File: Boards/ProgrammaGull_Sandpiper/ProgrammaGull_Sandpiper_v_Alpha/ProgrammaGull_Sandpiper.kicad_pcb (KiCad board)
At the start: 4 copper layers, 100 x 75 mm, 191 parts, among them J4 Conn_01x22_Socket, P1 USB_C_Plug_USB2.0, Q1 MMBT2907, Q2 MMBT2907, Q3 MMBT2907, Q4 MMBT2907, Q5 MMBT2907, Q6 MMBT2907, Q7 MMBT2907, Q8 MMBT2907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

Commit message: Final Alpha Version
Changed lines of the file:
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@@
     (property "ki_keywords" "EEPROM memory Microwire")
     (attr smd)
-    (fp_text reference "U6" (at -2.7 -1.65 180) (layer "F.SilkS")
+    (fp_text reference "U6" (at 5.25 -6.8 180) (layer "F.SilkS")
         (effects (font (size 1 1) (thickness 0.15)))
     )
@@
     (property "ki_keywords" "HCMOS SR OpenCollector")
     (attr smd)
-    (fp_text reference "U3" (at 0 -3.45 90) (layer "F.SilkS")
+    (fp_text reference "U3" (at -1.6625 4.125 -180) (layer "F.SilkS")
         (effects (font (size 1 1) (thickness 0.15)))
     )

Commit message: Final Sandpiper Alpha Changes, just cleanup.
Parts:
- moved C33 1.95 mm to (94.5, 55.8)
- moved C32 1.80 mm to (92.5, 56.0)
- turned C3 to -90 degrees
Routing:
- net GND: track 119.4 -> 114.3 mm

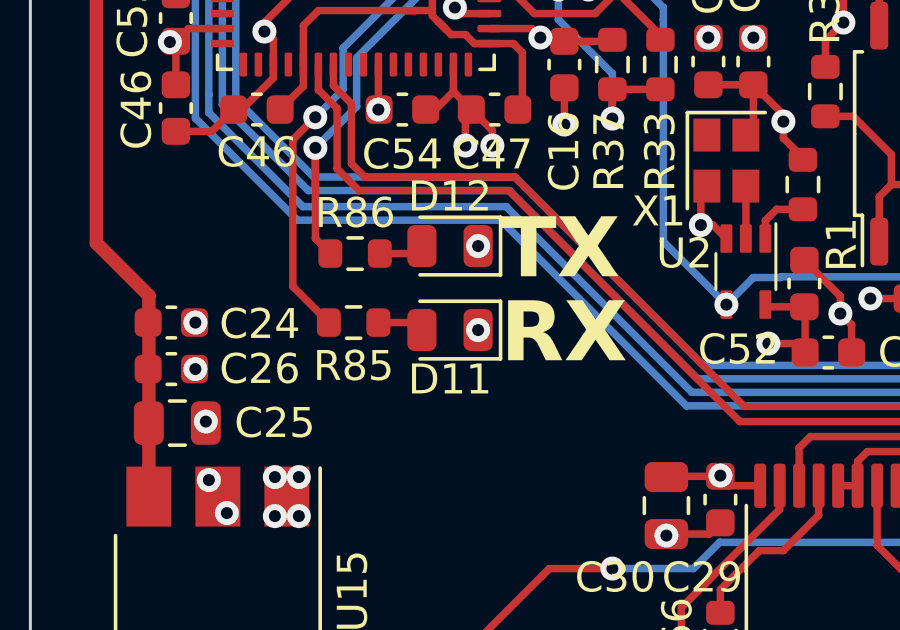
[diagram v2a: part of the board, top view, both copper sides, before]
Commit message: Errata: Fixed reversed LEDs on FTDI.... oops :)
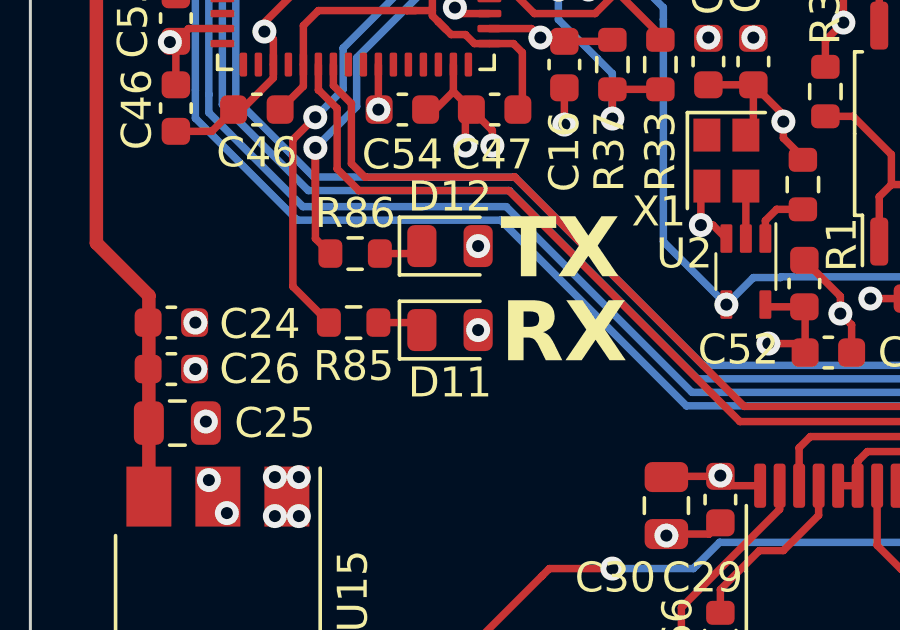
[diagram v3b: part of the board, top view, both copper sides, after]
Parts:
- turned D11 to 0 degrees
- turned D12 to 0 degrees
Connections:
- D11 pad 1: GND -> Net-(D11-K)
- D11 pad 2: Net-(D11-A) -> +3V3
- D12 pad 1: GND -> Net-(D12-K)
- D12 pad 2: Net-(D12-A) -> +3V3
- R85 pad 1: Net-(D11-A) -> Net-(D11-K)
- R86 pad 1: Net-(D12-A) -> Net-(D12-K)
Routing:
- net Net-(D11-K): track 0.00 -> 1.55 mm
- net Net-(D11-A): track 1.55 -> 0.00 mm
- net Net-(D12-K): track 0.00 -> 1.50 mm
- net Net-(D12-A): track 1.50 -> 0.00 mm
- net GND: vias 96 -> 94
- net +3V3: vias 54 -> 56
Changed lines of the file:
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@@
   (net 164 "Net-(J4-Pin_11)")
   (net 165 "Net-(J4-Pin_12)")
-  (net 166 "Net-(D11-A)")
-  (net 167 "Net-(D12-A)")
+  (net 166 "Net-(D11-K)")
+  (net 167 "Net-(D12-K)")
   (net 168 "Net-(U7-BCBUS4)")
   (net 169 "Net-(U7-BCBUS3)")
@@
       (stroke (width 0.1) (type solid)) (layer "F.Fab"))
     (pad "1" smd roundrect (at -0.825 0 180) (size 0.8 0.95) (layers "F.Cu" "F.Paste" "F.Mask") (roundrect_rratio 0.25)
-      (net 166 "Net-(D11-A)") (pintype "passive"))
+      (net 166 "Net-(D11-K)") (pintype "passive"))
     (pad "2" smd roundrect (at 0.825 0 180) (size 0.8 0.95) (layers "F.Cu" "F.Paste" "F.Mask") (roundrect_rratio 0.25)
       (net 168 "Net-(U7-BCBUS4)") (pintype "passive"))
@@
   )
   (footprint "LED_SMD:LED_0805_2012Metric" (layer "F.Cu")
-    (at 38.9875 64.25 180)
+    (at 38.9875 64.25)
     (descr "LED SMD 0805 (2012 Metric), square (rectangular) end terminal, IPC_7351 nominal, (Body size source: https://docs.google.com/spreadsheets/d/1BsfQQcO9C6DZCsRaXUlFlo91Tg2WpOkGARC1WS5S8t0/edit?usp=sharing), generated with kicad-footprint-generator")
     (tags "LED")
@@
     (property "ki_keywords" "LED diode")
     (attr smd)
-    (fp_text reference "D11" (at 0 -1.65) (layer "F.SilkS")
+    (fp_text reference "D11" (at 0 1.75) (layer "F.SilkS")
         (effects (font (size 1 1) (thickness 0.15)))
     )
@@
     (fp_line (start 1 0.6) (end 1 -0.6)
       (stroke (width 0.1) (type solid)) (layer "F.Fab"))
-    (pad "1" smd roundrect (at -0.9375 0 180) (size 0.975 1.4) (layers "F.Cu" "F.Paste" "F.Mask") (roundrect_rratio 0.25)
-      (net 2 "GND") (pinfunction "K") (pintype "passive"))
-    (pad "2" smd roundrect (at 0.9375 0 180) (size 0.975 1.4) (layers "F.Cu" "F.Paste" "F.Mask") (roundrect_rratio 0.25)
-      (net 166 "Net-(D11-A)") (pinfunction "A") (pintype "passive"))
+    (pad "1" smd roundrect (at -0.9375 0) (size 0.975 1.4) (layers "F.Cu" "F.Paste" "F.Mask") (roundrect_rratio 0.25)
+      (net 166 "Net-(D11-K)") (pinfunction "K") (pintype "passive"))
+    (pad "2" smd roundrect (at 0.9375 0) (size 0.975 1.4) (layers "F.Cu" "F.Paste" "F.Mask") (roundrect_rratio 0.25)
+      (net 3 "+3V3") (pinfunction "A") (pintype "passive"))
     (model "${KICAD6_3DMODEL_DIR}/LED_SMD.3dshapes/LED_0805_2012Metric.wrl"
       (offset (xyz 0 0 0))
@@
       (stroke (width 0.1) (type solid)) (layer "F.Fab"))
     (pad "1" smd roundrect (at -0.825 0 180) (size 0.8 0.95) (layers "F.Cu" "F.Paste" "F.Mask") (roundrect_rratio 0.25)
-      (net 167 "Net-(D12-A)") (pintype "passive"))
+      (net 167 "Net-(D12-K)") (pintype "passive"))
     (pad "2" smd roundrect (at 0.825 0 180) (size 0.8 0.95) (layers "F.Cu" "F.Paste" "F.Mask") (roundrect_rratio 0.25)
       (net 169 "Net-(U7-BCBUS3)") (pintype "passive"))
@@
   )
   (footprint "LED_SMD:LED_0805_2012Metric" (layer "F.Cu")
-    (at 38.9875 61.45 180)
+    (at 38.9875 61.45)
     (descr "LED SMD 0805 (2012 Metric), square (rectangular) end terminal, IPC_7351 nominal, (Body size source: https://docs.google.com/spreadsheets/d/1BsfQQcO9C6DZCsRaXUlFlo91Tg2WpOkGARC1WS5S8t0/edit?usp=sharing), generated with kicad-footprint-generator")
     (tags "LED")
@@
     (property "ki_keywords" "LED diode")
     (attr smd)
-    (fp_text reference "D12" (at 0 1.65) (layer "F.SilkS")
+    (fp_text reference "D12" (at 0 -1.65) (layer "F.SilkS")
         (effects (font (size 1 1) (thickness 0.15)))
     )
@@
     (fp_line (start 1 0.6) (end 1 -0.6)
       (stroke (width 0.1) (type solid)) (layer "F.Fab"))
-    (pad "1" smd roundrect (at -0.9375 0 180) (size 0.975 1.4) (layers "F.Cu" "F.Paste" "F.Mask") (roundrect_rratio 0.25)
-      (net 2 "GND") (pinfunction "K") (pintype "passive"))
-    (pad "2" smd roundrect (at 0.9375 0 180) (size 0.975 1.4) (layers "F.Cu" "F.Paste" "F.Mask") (roundrect_rratio 0.25)
-      (net 167 "Net-(D12-A)") (pinfunction "A") (pintype "passive"))
+    (pad "1" smd roundrect (at -0.9375 0) (size 0.975 1.4) (layers "F.Cu" "F.Paste" "F.Mask") (roundrect_rratio 0.25)
+      (net 167 "Net-(D12-K)") (pinfunction "K") (pintype "passive"))
+    (pad "2" smd roundrect (at 0.9375 0) (size 0.975 1.4) (layers "F.Cu" "F.Paste" "F.Mask") (roundrect_rratio 0.25)
+      (net 3 "+3V3") (pinfunction "A") (pintype "passive"))
     (model "${KICAD6_3DMODEL_DIR}/LED_SMD.3dshapes/LED_0805_2012Metric.wrl"
       (offset (xyz 0 0 0))
@@
   (via (at 35.15 52.75) (size 0.8) (drill 0.4) (layers "F.Cu" "B.Cu") (net 2))
   (via (at 38.6 40.6) (size 0.8) (drill 0.4) (layers "F.Cu" "B.Cu") (free) (net 2))
-  (via (at 39.925 64.25) (size 0.8) (drill 0.4) (layers "F.Cu" "B.Cu") (net 2))
   (via (at 39.5 58.1) (size 0.8) (drill 0.4) (layers "F.Cu" "B.Cu") (free) (net 2))
   (via (at 71 76.1) (size 0.8) (drill 0.4) (layers "F.Cu" "B.Cu") (net 2))
@@
   (via (at 58.6 61.3) (size 0.8) (drill 0.4) (layers "F.Cu" "B.Cu") (free) (net 2))
   (via (at 112.3975 76.33) (size 0.8) (drill 0.4) (layers "F.Cu" "B.Cu") (free) (net 2))
-  (via (at 39.925 61.45) (size 0.8) (drill 0.4) (layers "F.Cu" "B.Cu") (net 2))
   (via (at 78.3 72.9) (size 0.8) (drill 0.4) (layers "F.Cu" "B.Cu") (net 2))
   (via (at 66.5 83.3) (size 0.8) (drill 0.4) (layers "F.Cu" "B.Cu") (net 2))
@@
   (via (at 41.95 39.35) (size 0.8) (drill 0.4) (layers "F.Cu" "B.Cu") (free) (net 3))
   (via (at 67.1 74.3) (size 0.8) (drill 0.4) (layers "F.Cu" "B.Cu") (net 3))
+  (via (at 39.925 64.25) (size 0.8) (drill 0.4) (layers "F.Cu" "B.Cu") (net 3))
   (via (at 118.1 86.9) (size 0.8) (drill 0.4) (layers "F.Cu" "B.Cu") (net 3))
   (via (at 59.925 75) (size 0.8) (drill 0.4) (layers "F.Cu" "B.Cu") (free) (net 3))
@@
   (via (at 55.2 70.6) (size 0.8) (drill 0.4) (layers "F.Cu" "B.Cu") (net 3))
   (via (at 30.65 75.55) (size 0.8) (drill 0.4) (layers "F.Cu" "B.Cu") (net 3))
+  (via (at 39.925 61.45) (size 0.8) (drill 0.4) (layers "F.Cu" "B.Cu") (net 3))
   (via (at 76.7 72.9) (size 0.8) (drill 0.4) (layers "F.Cu" "B.Cu") (net 3))
   (via (at 59.725 71.65) (size 0.8) (drill 0.4) (layers "F.Cu" "B.Cu") (net 3))

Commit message: Updated board revision for Alpha
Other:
- board text added: "Version: Alpha 0.2"
- board text removed: "Version: Alpha 0.1"
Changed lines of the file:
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@@
     (effects (font (size 1.5 1.5) (thickness 0.3) bold) (justify left bottom mirror))
   )
-  (gr_text "Version: Alpha 0.1" (at 95 75.45) (layer "B.SilkS")
+  (gr_text "Version: Alpha 0.2" (at 95 75.45) (layer "B.SilkS")
     (effects (font (size 2 2) (thickness 0.3) bold) (justify left bottom mirror))
   )

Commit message: Minor Adds, small fixes on Sandpiper PCB
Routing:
- net /UI_MSB_CA1: track 8.11 -> 5.57 mm
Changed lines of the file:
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@@
   (segment (start 50.2 31.5) (end 51.96 29.74) (width 0.25) (layer "F.Cu") (net 32))
   (segment (start 49.3 45.4375) (end 49.3 46.5) (width 0.25) (layer "F.Cu") (net 33))
-  (segment (start 51.4 49.1) (end 49.6 47.3) (width 0.25) (layer "F.Cu") (net 33))
   (segment (start 49.3 46.5) (end 49.6 46.8) (width 0.25) (layer "F.Cu") (net 33))
   (segment (start 49.6 46.8) (end 49.6 47.3) (width 0.25) (layer "F.Cu") (net 33))

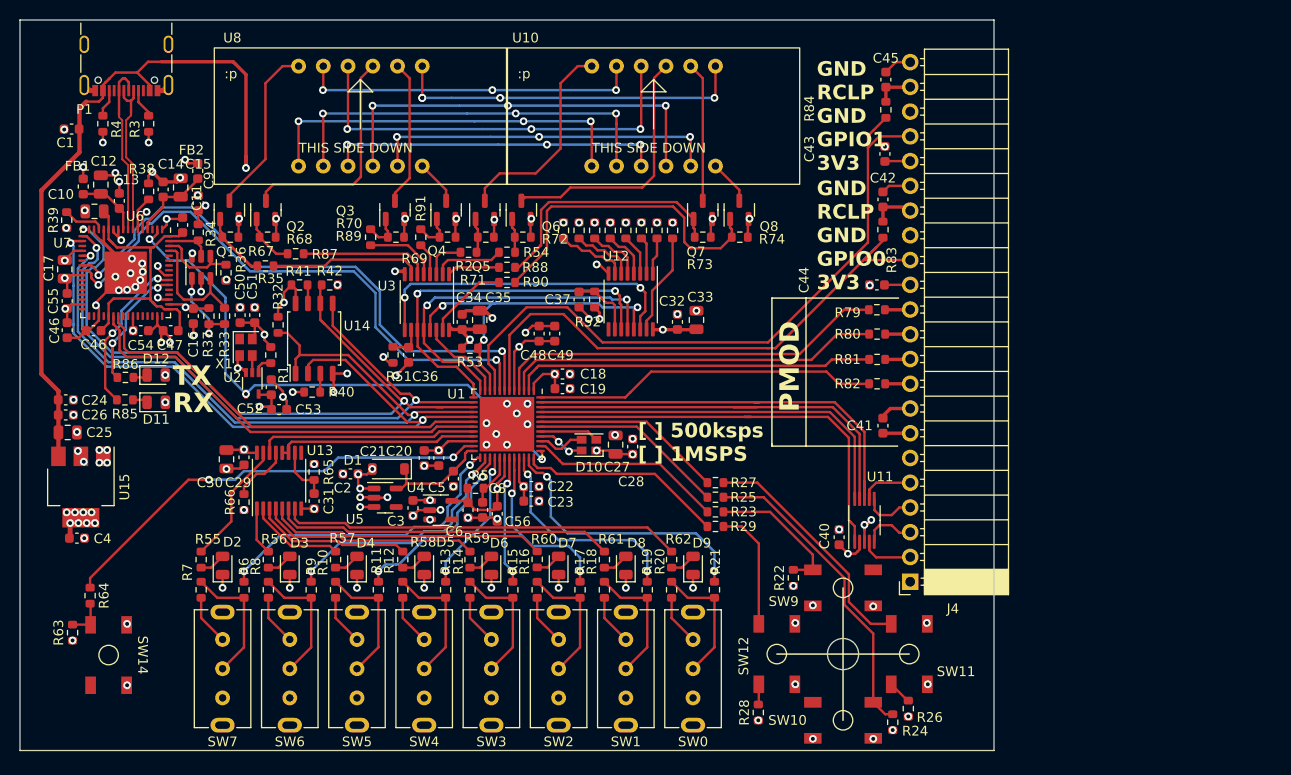
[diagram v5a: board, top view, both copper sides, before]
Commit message: In progress conversion to maintaining 5V on seven segment
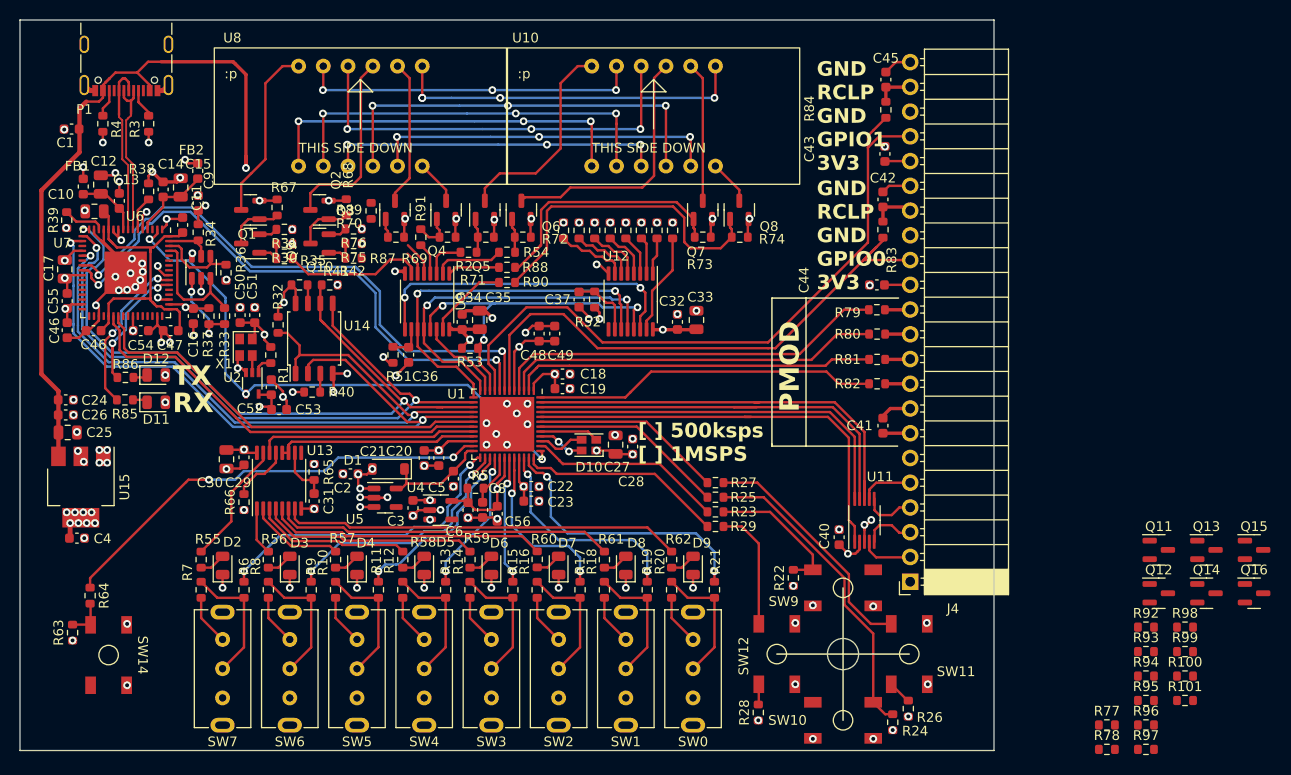
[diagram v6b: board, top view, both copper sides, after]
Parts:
- removed U3: 74HC596, Package_SO:TSSOP-16_4.4x5mm_P0.65mm
- added Q10: MMBT3904, Package_TO_SOT_SMD:SOT-23, F.Cu at (55.8, 48.0)
- added Q11: MMBT3904, Package_TO_SOT_SMD:SOT-23, F.Cu at (141.9, 79.4)
- added Q12: MMBT3904, Package_TO_SOT_SMD:SOT-23, F.Cu at (141.9, 83.9)
- added Q13: MMBT3904, Package_TO_SOT_SMD:SOT-23, F.Cu at (146.8, 79.4)
- added Q14: MMBT3904, Package_TO_SOT_SMD:SOT-23, F.Cu at (146.8, 83.9)
- added Q15: MMBT3904, Package_TO_SOT_SMD:SOT-23, F.Cu at (151.7, 79.4)
- added Q16: MMBT3904, Package_TO_SOT_SMD:SOT-23, F.Cu at (151.7, 83.9)
- added Q9: MMBT3904, Package_TO_SOT_SMD:SOT-23, F.Cu at (48.6, 48.0)
- added R100: 10k, Resistor_SMD:R_0603_1608Metric, F.Cu at (144.6, 92.4)
- added R101: 10k, Resistor_SMD:R_0603_1608Metric, F.Cu at (144.6, 94.9)
- added R30: 10k, Resistor_SMD:R_0603_1608Metric, F.Cu at (52.1, 48.0)
- added R31: 10k, Resistor_SMD:R_0603_1608Metric, F.Cu at (52.1, 46.5)
- added R75: 10k, Resistor_SMD:R_0603_1608Metric, F.Cu at (59.2, 48.0)
- added R76: 10k, Resistor_SMD:R_0603_1608Metric, F.Cu at (59.2, 46.5)
- added R77: 10k, Resistor_SMD:R_0603_1608Metric, F.Cu at (136.6, 97.4)
- added R78: 10k, Resistor_SMD:R_0603_1608Metric, F.Cu at (136.6, 99.9)
- added R92: 10k, Resistor_SMD:R_0603_1608Metric, F.Cu at (140.6, 87.3)
- added R93: 10k, Resistor_SMD:R_0603_1608Metric, F.Cu at (140.6, 89.8)
- added R94: 10k, Resistor_SMD:R_0603_1608Metric, F.Cu at (140.6, 92.4)
- added R95: 10k, Resistor_SMD:R_0603_1608Metric, F.Cu at (140.6, 94.9)
- added R96: 10k, Resistor_SMD:R_0603_1608Metric, F.Cu at (140.6, 97.4)
- added R97: 10k, Resistor_SMD:R_0603_1608Metric, F.Cu at (140.6, 99.9)
- added R98: 10k, Resistor_SMD:R_0603_1608Metric, F.Cu at (144.6, 87.3)
- added R99: 10k, Resistor_SMD:R_0603_1608Metric, F.Cu at (144.6, 89.8)
- added U9: 74AHC595, Package_SO:TSSOP-16_4.4x5mm_P0.65mm, F.Cu at (66.8, 53.9)
- moved R68 8.64 mm to (58.5, 44.2), turned to 90 degrees
- moved R87 5.97 mm to (59.2, 49.5)
- moved R67 5.69 mm to (51.4, 44.2), turned to 90 degrees
- moved Q2 5.50 mm to (55.8, 44.5), turned to 180 degrees
- moved R89 2.70 mm to (61.0, 44.6)
- moved Q1 2.15 mm to (48.6, 44.5), turned to 180 degrees
- moved R35 2.09 mm to (52.1, 49.5)
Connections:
- Q1 pad 1: /UI_MSB_CA0 -> /CA0_MSB_BASE
- Q2 pad 1: /UI_MSB_CA1 -> /CA1_MSB_BASE
- Q3 pad 1: /UI_MSB_CA2 -> /CA2_MSB_BASE
- Q4 pad 1: /UI_MSB_CA3 -> /CA3_MSB_BASE
- Q5 pad 1: /UI_LSB_CA0 -> /CA0_LSB_BASE
- Q6 pad 1: /UI_LSB_CA1 -> /CA1_LSB_BASE
- Q7 pad 1: /UI_LSB_CA2 -> /CA2_LSB_BASE
- Q8 pad 1: /UI_LSB_CA3 -> /CA3_LSB_BASE
- R67 pad 1: /UI_MSB_CA0 -> /CA0_MSB_BASE
- R68 pad 1: /UI_MSB_CA1 -> /CA1_MSB_BASE
- R69 pad 1: /UI_MSB_CA3 -> /CA3_MSB_BASE
- R70 pad 1: /UI_MSB_CA2 -> /CA2_MSB_BASE
- R71 pad 1: /UI_LSB_CA0 -> /CA0_LSB_BASE
- R72 pad 1: /UI_LSB_CA1 -> /CA1_LSB_BASE
- R73 pad 1: /UI_LSB_CA2 -> /CA2_LSB_BASE
- R74 pad 1: /UI_LSB_CA3 -> /CA3_LSB_BASE
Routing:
- net Net-(U9-QG): track 13.1 -> 2.46 mm
- net /CA0_MSB_BASE: track 0.00 -> 5.91 mm
- net /CA1_MSB_BASE: track 0.00 -> 5.86 mm
- net /UI_MSB_CA2: track 4.07 -> 0.00 mm
- net Net-(U9-QF): track 7.42 -> 3.60 mm
- net Net-(Q2-C): track 23.2 -> 19.5 mm
- net /UI_MSB_CA0: track 6.78 -> 3.49 mm
- net /UI_MSB_CA1: track 5.57 -> 3.45 mm
- net /CA2_MSB_BASE: track 0.00 -> 1.96 mm
- net Net-(Q10-E): track 0.00 -> 1.95 mm
- net Net-(Q9-E): track 0.00 -> 1.94 mm
- net Net-(U9-QH): track 15.4 -> 14.5 mm
- net GND: vias 94 -> 98
